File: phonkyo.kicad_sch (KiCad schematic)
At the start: 30 parts, among them J1 GPIO, J2 LineOutJack, J4 RIJack, U1 CAT24C256, U2 PCM5102A, U3 XC6206P332MR

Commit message: add: C14, 100 nF decoupling on DAC AVDD (pin 8)
AVDD (U2 pin 8) had no local decoupling. It was fed from beside pin 1
through a via and a B.Cu detour, about 9 mm from any capacitor. TI's
reference layout decouples CPVDD (pin 1) and AVDD (pin 8) separately.

C14 is a 100 nF 0402 at (146.2, 90.6), about 1.6 mm from pin 8. Its GNDA
pad sits in the analog pour. In the schematic it is the third cap on the
LDO output rails, beside C7 and C8, with its own junctions.

U2 pad 9 (AGND) is switched to a solid zone connection. Pin 9 is
wedged between pins 8 and 10, so it can only take thermal spokes to the
left and right. Decoupling pin 8 from the left necessarily uses its
left spoke, which left 1 spoke and a DRC starved-thermal error. A solid
connection is normal for a reflowed ground pin and gives AGND a
lower-impedance path. This is a per-pad override; no other pad changes.

Verified: ERC shows no new errors, and C14's nets are confirmed from
the exported netlist (pin 1 GNDA, pin 2 +3.3VA). DRC with schematic
parity: 0 unconnected, 0 parity errors, no new violations. Semantic
diff: C14 added, no other footprint moved, 2 new +3.3VA tracks, and the
pad 9 override.

Co-Authored-By: Claude Opus 5.5 <noreply@anthropic.com>
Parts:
- added C14: 0.1u, Capacitor_SMD:C_0402_1005Metric, symbol Device:C_Small
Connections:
- net +3.3VA: now also C14.2
- net GNDA: now also C14.1
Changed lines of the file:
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@@
 	(wire
 		(pts
+			(xy 210.82 120.65) (xy 213.36 120.65)
+		)
+		(stroke
+			(width 0)
+			(type default)
+		)
+	)
+	(wire
+		(pts
+			(xy 213.36 120.65) (xy 213.36 123.19)
+		)
+		(stroke
+			(width 0)
+			(type default)
+		)
+	)
+	(wire
+		(pts
+			(xy 204.47 128.27) (xy 213.36 128.27)
+		)
+		(stroke
+			(width 0)
+			(type default)
+		)
+	)
+	(junction
+		(at 210.82 120.65)
+		(diameter 0)
+		(color 0 0 0 0)
+	)
+	(junction
+		(at 204.47 128.27)
+		(diameter 0)
+		(color 0 0 0 0)
+	)
+	(wire
+		(pts
 			(xy 58.42 58.42) (xy 58.42 76.2)
 		)
@@
 					(unit 1)
 				)
+			)
+		)
+	)
+	(symbol
+		(lib_id "Device:C_Small")
+		(at 213.36 125.73 180)
+		(unit 1)
+		(body_style 1)
+		(exclude_from_sim no)
+		(in_bom yes)
+		(on_board yes)
+		(in_pos_files yes)
+		(dnp no)
+		(fields_autoplaced yes)
+		(property "Reference" "C14"
+			(at 215.90 124.4535 0)
+			(show_name no)
+			(do_not_autoplace no)
+			(effects
+				(font
+					(size 1.27 1.27)
+				)
+				(justify right)
+			)
+		)
+		(property "Value" "0.1u"
+			(at 215.90 126.9935 0)
+			(show_name no)
+			(do_not_autoplace no)
+			(effects
+				(font
+					(size 1.27 1.27)
+				)
+				(justify right)
+			)
+		)
+		(property "Footprint" "Capacitor_SMD:C_0402_1005Metric"
+			(at 213.36 125.73 0)
+			(hide yes)
+			(show_name no)
+			(do_not_autoplace no)
+			(effects
+				(font
+					(size 1.27 1.27)
+				)
+			)
+		)
+		(property "Datasheet" ""
+			(at 213.36 125.73 0)
+			(hide yes)
+			(show_name no)
+			(do_not_autoplace no)
+			(effects
+				(font
+					(size 1.27 1.27)
+				)
+			)
+		)
+		(property "Description" "Unpolarized capacitor, small symbol"
+			(at 213.36 125.73 0)
+			(hide yes)
+			(show_name no)
+			(do_not_autoplace no)
+			(effects
+				(font
+					(size 1.27 1.27)
+				)
+			)
+		)
+		(pin "1"
+		)
+		(pin "2"
+		)
+		(instances
+			(project "phonkyo"
+				(path "/e63e39d7-6ac0-4ffd-8aa3-1841a4541b55"
+					(reference "C14")
+					(unit 1)
+				)

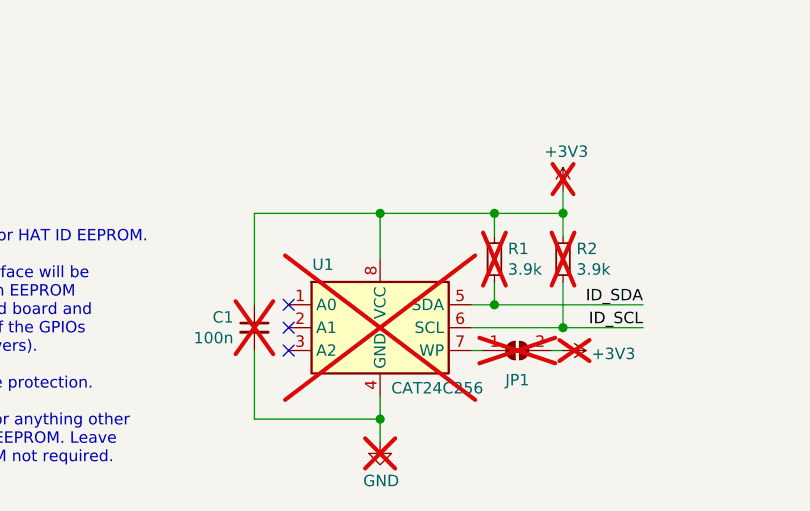
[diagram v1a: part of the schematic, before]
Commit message: add: HAT ID EEPROM (CAT24C256) with pull-ups, decoupling and WP jumper
Enables the previously DNP ID EEPROM circuit so the Pi can identify the
board and load its overlay at boot:

- U1 CAT24C256, TSSOP-8, in the strip above the 3.5 mm jacks
- R1/R2 3.9k pull-ups on ID_SD/ID_SC (HAT spec value), 0402
- C1 100 nF at VCC (pin 8), with its own GND via
- JP1 solder jumper on the bottom side: open = WP floats low
  (writable, for flashing), bridged = WP tied to +3V3 (protected)

Routing is by hand. Both ID lines stay on F.Cu from the header: ID_SC
along the board edge above the header, ID_SD between the header rows.
B.Cu is used only for short vertical hops under the +3V3/+5V rails,
plus a +3V3 hop from the rail. The existing GPIO25 route is untouched.
The B.Cu GND pour stays a single piece (1733 -> 1715 mm2).

DRC with schematic parity: 0 unconnected, 0 parity, no errors; only
library-mismatch warnings, where C1/R1/R2 inherit them from the existing
0402 footprints they were cloned from. ERC is unchanged. No
pre-existing track, via or footprint is moved.

Co-Authored-By: Claude Opus 5.5 <noreply@anthropic.com>
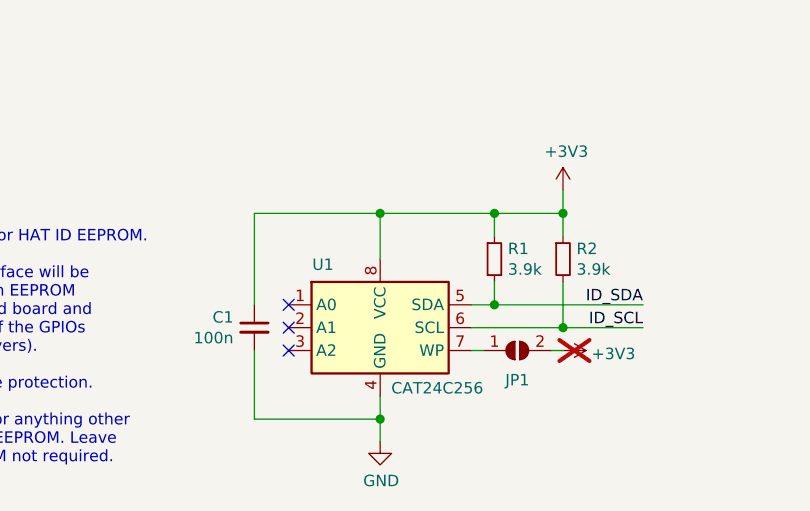
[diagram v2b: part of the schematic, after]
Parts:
- C1: footprint (none) -> Capacitor_SMD:C_0402_1005Metric; now fitted; now in the parts list
- JP1: footprint (none) -> Jumper:SolderJumper-2_P1.3mm_Open_Pad1.0x1.5mm; now fitted
- R1, R2: footprint (none) -> Resistor_SMD:R_0402_1005Metric; now fitted; now in the parts list
- U1: footprint (none) -> Package_SO:TSSOP-8_4.4x3mm_P0.65mm; now fitted; now in the parts list
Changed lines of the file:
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@@
 		(body_style 1)
 		(exclude_from_sim yes)
-		(in_bom no)
-		(on_board no)
+		(in_bom yes)
+		(on_board yes)
 		(in_pos_files yes)
-		(dnp yes)
+		(dnp no)
 		(property "Reference" "C1"
 			(at 64.9858 176.6506 0)
@@
 			)
 		)
-		(property "Footprint" ""
+		(property "Footprint" "Capacitor_SMD:C_0402_1005Metric"
 			(at 67.31 177.8 0)
 			(hide yes)
@@
 		(body_style 1)
 		(exclude_from_sim yes)
-		(in_bom no)
-		(on_board no)
+		(in_bom yes)
+		(on_board yes)
 		(in_pos_files yes)
-		(dnp yes)
+		(dnp no)
 		(property "Reference" "R1"
 			(at 95.4786 169.037 0)
@@
 			)
 		)
-		(property "Footprint" ""
+		(property "Footprint" "Resistor_SMD:R_0402_1005Metric"
 			(at 93.98 170.18 0)
 			(hide yes)
@@
 		(exclude_from_sim yes)
 		(in_bom no)
-		(on_board no)
-		(in_pos_files yes)
-		(dnp yes)
+		(on_board yes)
+		(in_pos_files no)
+		(dnp no)
 		(property "Reference" "JP1"
 			(at 96.52 183.623 0)
@@
 			)
 		)
-		(property "Footprint" ""
+		(property "Footprint" "Jumper:SolderJumper-2_P1.3mm_Open_Pad1.0x1.5mm"
 			(at 96.52 180.34 0)
 			(hide yes)
@@
 		(body_style 1)
 		(exclude_from_sim yes)
-		(in_bom no)
-		(on_board no)
+		(in_bom yes)
+		(on_board yes)
 		(in_pos_files yes)
-		(dnp yes)
+		(dnp no)
 		(property "Reference" "R2"
 			(at 103.0986 169.037 0)
@@
 			)
 		)
-		(property "Footprint" ""
+		(property "Footprint" "Resistor_SMD:R_0402_1005Metric"
 			(at 101.6 170.18 0)
 			(hide yes)
@@
 		(on_board no)
 		(in_pos_files yes)
-		(dnp yes)
+		(dnp no)
 		(property "Reference" "#PWR0101"
 			(at 101.6 166.37 0)
@@
 		(body_style 1)
 		(exclude_from_sim yes)
-		(in_bom no)
-		(on_board no)
+		(in_bom yes)
+		(on_board yes)
 		(in_pos_files yes)
-		(dnp yes)
+		(dnp no)
 		(property "Reference" "U1"
 			(at 74.93 170.7958 0)
@@
 			)
 		)
-		(property "Footprint" ""
+		(property "Footprint" "Package_SO:TSSOP-8_4.4x3mm_P0.65mm"
 			(at 81.28 177.8 0)
 			(hide yes)
@@
 		(on_board no)
 		(in_pos_files yes)
-		(dnp yes)
+		(dnp no)
 		(property "Reference" "#PWR0102"
 			(at 81.28 196.85 0)

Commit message: production: v0.3 fabrication and JLCPCB assembly files
- Plot output now goes to production/v0.3 instead of overwriting v0.2.
- Every fitted part has an LCSC field, in the schematic and on the PCB
  footprints, so the JLC BOM regenerates from the design. Basic parts are
  used wherever one fits. Extended picks: C0G for the 2.2 nF audio filter
  caps, 10 V for the 2.2 uF charge-pump caps, 3.9k 1% HAT pull-ups.
- production/v0.3: Gerbers (with F.Paste for the stencil), Excellon
  drills, JLC-format BOM and CPL, and a README with order settings. The
  CPL places J1 at its centre rather than its pin-1 anchor.

DRC with parity unchanged (0 unconnected, 0 parity, library warnings
only). No copper changed.

Co-Authored-By: Claude Opus 5.5 <noreply@anthropic.com>
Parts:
- C1, C11, C12, C14: LCSC (none) -> C1525
- C10, C4: LCSC (none) -> C107369
- C13, C8, C9: LCSC (none) -> C19702
- C2, C3, C6: LCSC (none) -> C385029
- C5: LCSC (none) -> C15849
- C7: LCSC (none) -> C14663
- J1: LCSC (none) -> C5124634
- J2, J4: LCSC (none) -> C95562
- R1, R2: LCSC (none) -> C131467
- R11: LCSC (none) -> C17168
- R3, R4: LCSC (none) -> C25117
- R5: LCSC (none) -> C25744
- R6: LCSC (none) -> C25765
- R7, R8, R9: LCSC (none) -> C25092
- U1: LCSC (none) -> C146734
- U2: LCSC (none) -> C107671
- U3: LCSC (none) -> C5446
